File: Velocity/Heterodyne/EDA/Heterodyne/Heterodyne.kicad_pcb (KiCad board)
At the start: 2 copper layers, 39.5 x 29.5 mm, 40 parts, among them J1 I2C, J3 PWR, J4 Doppler_Out, J5 V_Square, J7 Reciever, U1 SA612AD, U2 NE5532, U3 MAX7375AXR105, U4 MAX11613

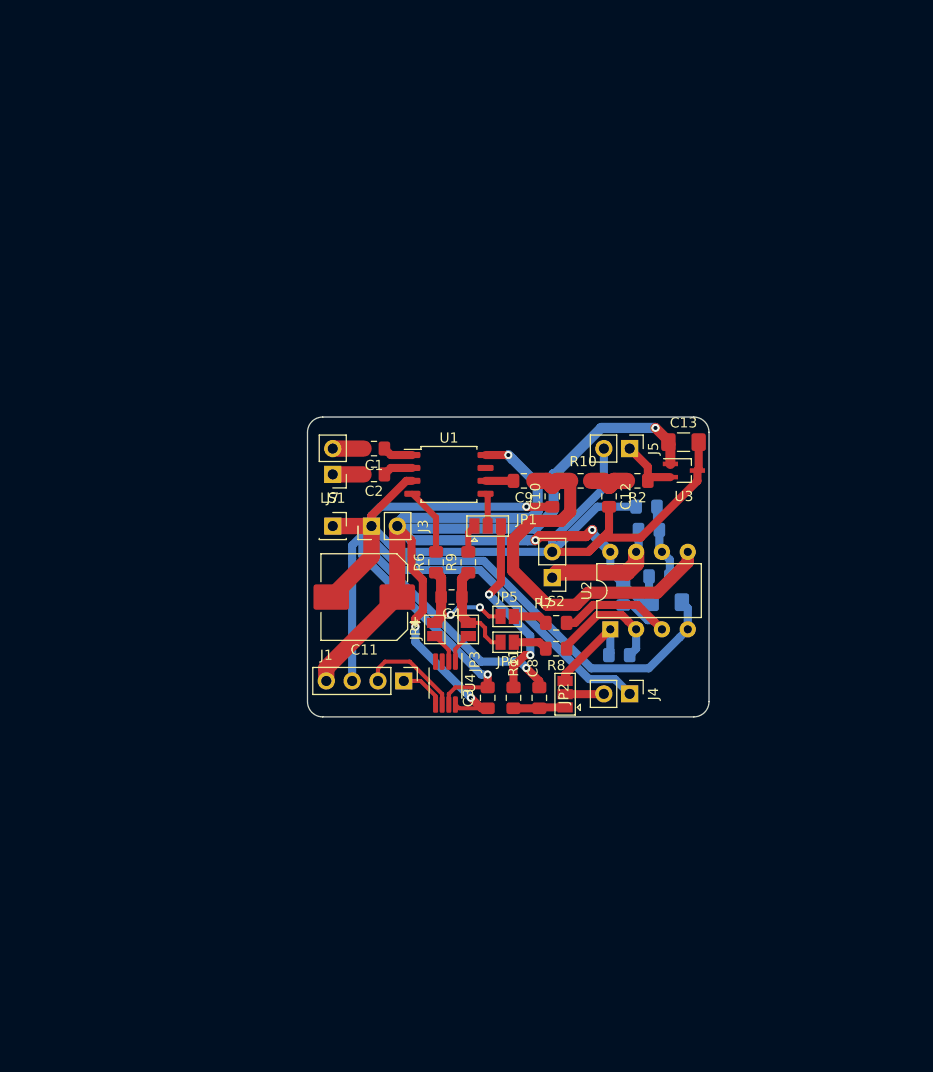
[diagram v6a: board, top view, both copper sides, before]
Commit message: added  ATmega328P to velocity schematic
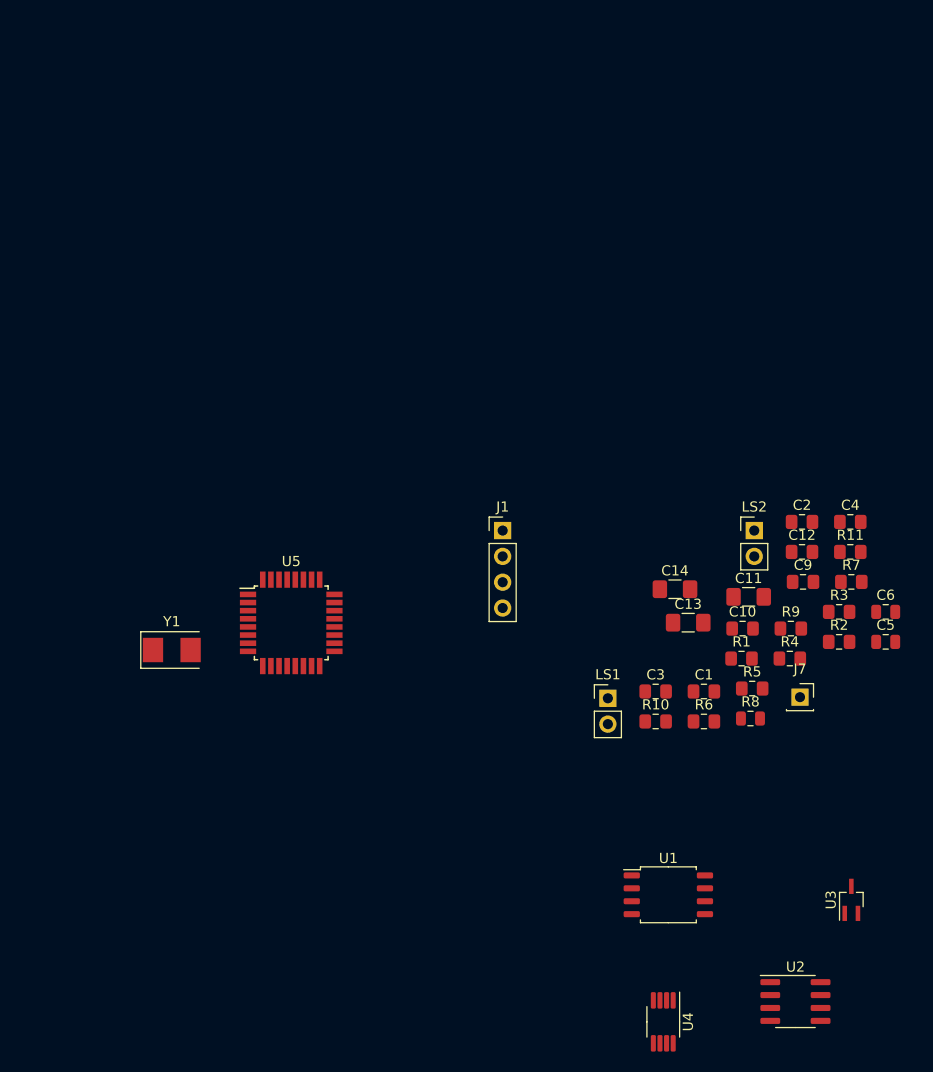
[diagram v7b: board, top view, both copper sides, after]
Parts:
- removed C8: 22 nF, Capacitor_SMD:C_0805_2012Metric_Pad1.15x1.40mm_HandSolder
- removed J3: PWR, Connector_PinHeader_2.54mm:PinHeader_1x02_P2.54mm_Vertical
- removed J4: Doppler_Out, Connector_PinHeader_2.54mm:PinHeader_1x02_P2.54mm_Vertical
- removed J5: V_Square, Connector_PinHeader_2.54mm:PinHeader_1x02_P2.54mm_Vertical
- removed JP1, JP2: Jumper_NC_Dual, Jumper:SolderJumper-3_P1.3mm_Open_Pad1.0x1.5mm
- removed JP3, JP4, JP5, JP6: SolderJumper_2_Open, Jumper:SolderJumper-2_P1.3mm_Open_Pad1.0x1.5mm
- removed R12: 18 kΩ, Resistor_SMD:R_0805_2012Metric_Pad1.15x1.40mm_HandSolder
- added C5: 22 nF, Capacitor_SMD:C_0805_2012Metric, F.Cu at (188.4, 97.1)
- added C6: 22 nF, Capacitor_SMD:C_0805_2012Metric, F.Cu at (188.4, 94.2)
- added U5: ATmega328PB-AU, Package_QFP:TQFP-32_7x7mm_P0.8mm, F.Cu at (129.9, 95.2)
- added Y1: 8 MHz, Crystal:Crystal_SMD_5032-2Pin_5.0x3.2mm, F.Cu at (118.2, 97.9)
- C11: value 330 μF -> 3.3 μF; footprint Capacitor_SMD:CP_Elec_8x10 -> Capacitor_SMD:C_1206_3216Metric_Pad1.42x1.75mm_HandSolder
- C14, R1, R3, R4: moved to F.Cu
- R11: value 330 Ω -> 20 kΩ
- R5: value 18 kΩ -> 2 kΩ; moved to F.Cu
- R6: value 330 Ω -> 1 kΩ
- R7: value 1 kΩ -> 330 Ω
- R8: value 1 kΩ -> 10 kΩ; footprint Resistor_SMD:R_0805_2012Metric_Pad1.15x1.40mm_HandSolder -> Resistor_SMD:R_0805_2012Metric
- U2: value NE5532 -> NE5532DR; footprint Package_DIP:DIP-8_W7.62mm -> Package_SO:SOIC-8_3.9x4.9mm_P1.27mm
- moved J7 49.0 mm to (179.9, 102.6)
- moved U1 46.6 mm to (167.0, 122.0)
- moved U3 45.3 mm to (185.0, 122.5), turned to 90 degrees
- moved C2 42.4 mm to (180.2, 85.3), turned to 0 degrees
- moved U2 40.9 mm to (179.5, 132.5), turned to 0 degrees
- moved C1 40.3 mm to (170.5, 102.0), turned to 0 degrees
- moved C4 39.9 mm to (184.9, 85.3), turned to 0 degrees
- moved U4 39.6 mm to (166.5, 134.5)
- moved C11 37.8 mm to (174.9, 92.7), turned to 0 degrees
- moved R11 36.1 mm to (184.9, 88.3), turned to 0 degrees
- moved LS1 34.9 mm to (161.1, 102.7), turned to 0 degrees
- moved R9 32.4 mm to (179.1, 95.8), turned to 0 degrees
- moved R6 30.7 mm to (170.5, 105.0), turned to 0 degrees
- moved R7 29.3 mm to (185.0, 91.2), turned to 0 degrees
- moved C9 29.2 mm to (180.2, 91.2), turned to 0 degrees
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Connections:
- C13 pad 2: VPP -> VCLOCK
- C14 pad 1: VPP -> VOPAMP
- J1 pad 1: Net-(J1-Pad1) -> BCLOCK
- J1 pad 2: Net-(J1-Pad2) -> BDATA
- R11 pad 1: Net-(C8-Pad1) -> SDA
- R11 pad 2: Net-(JP1-Pad3) -> VPP
- R5 pad 1: Net-(R5-Pad1) -> VPP
- R5 pad 2: VPP -> Net-(R5-Pad2)
- R6 pad 1: Net-(C4-Pad2) -> Net-(R5-Pad2)
- R6 pad 2: Net-(R6-Pad2) -> GND
- R7 pad 1: Net-(R5-Pad1) -> Net-(R7-Pad1)
- R7 pad 2: Net-(JP5-Pad2) -> Net-(C4-Pad1)
- R8 pad 1: Net-(R12-Pad1) -> VPP
- R9 pad 1: Net-(C4-Pad1) -> Net-(R9-Pad1)
- R9 pad 2: Net-(JP1-Pad1) -> Net-(C4-Pad2)
- U1 pad 4: Net-(R6-Pad2) -> Net-(R9-Pad1)
- U1 pad 5: Net-(JP1-Pad2) -> Net-(R7-Pad1)
- U2 pad 1: Net-(JP2-Pad3) -> (no net)
- U2 pad 2: Net-(R12-Pad1) -> (no net)
- U2 pad 3: Net-(R5-Pad1) -> (no net)
- U2 pad 8: VPP -> VOPAMP
- U3 pad 1: VPP -> VCLOCK
- U4 pad 1: Net-(JP3-Pad2) -> Net-(C4-Pad1)
- U4 pad 2: Net-(JP4-Pad2) -> Net-(C4-Pad2)
- U4 pad 4: Net-(U4-Pad4) -> Net-(R5-Pad2)
- U4 pad 5: Net-(J1-Pad1) -> SCL
- U4 pad 6: Net-(J1-Pad2) -> SDA
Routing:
- net GND: track 244.6 -> 0.00 mm, vias 3 -> 0
- net VPP: track 136.4 -> 0.00 mm, vias 6 -> 0
- net Driver_Wave: track 38.1 -> 0.00 mm
- net Net-(JP1-Pad3): track 19.0 -> 0.00 mm, vias 2 -> 0
- net Net-(R5-Pad1): track 15.9 -> 0.00 mm
- net Net-(LS2-Pad1): track 12.2 -> 0.00 mm
- net Net-(C4-Pad2): track 12.0 -> 0.00 mm, vias 2 -> 0
- net Net-(R12-Pad1): track 11.8 -> 0.00 mm
- net Net-(J1-Pad2): track 10.2 -> 0.00 mm
- net Net-(C4-Pad1): track 9.87 -> 0.00 mm
- net Net-(JP2-Pad3): track 9.52 -> 0.00 mm
- net Net-(R1-Pad2): track 7.38 -> 0.00 mm
- net Net-(R6-Pad2): track 6.68 -> 0.00 mm
- net Net-(R2-Pad1): track 6.28 -> 0.00 mm
- net Net-(C8-Pad1): track 5.12 -> 0.00 mm
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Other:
- board outline removed

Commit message: added 4 layer PCB for heterodyne
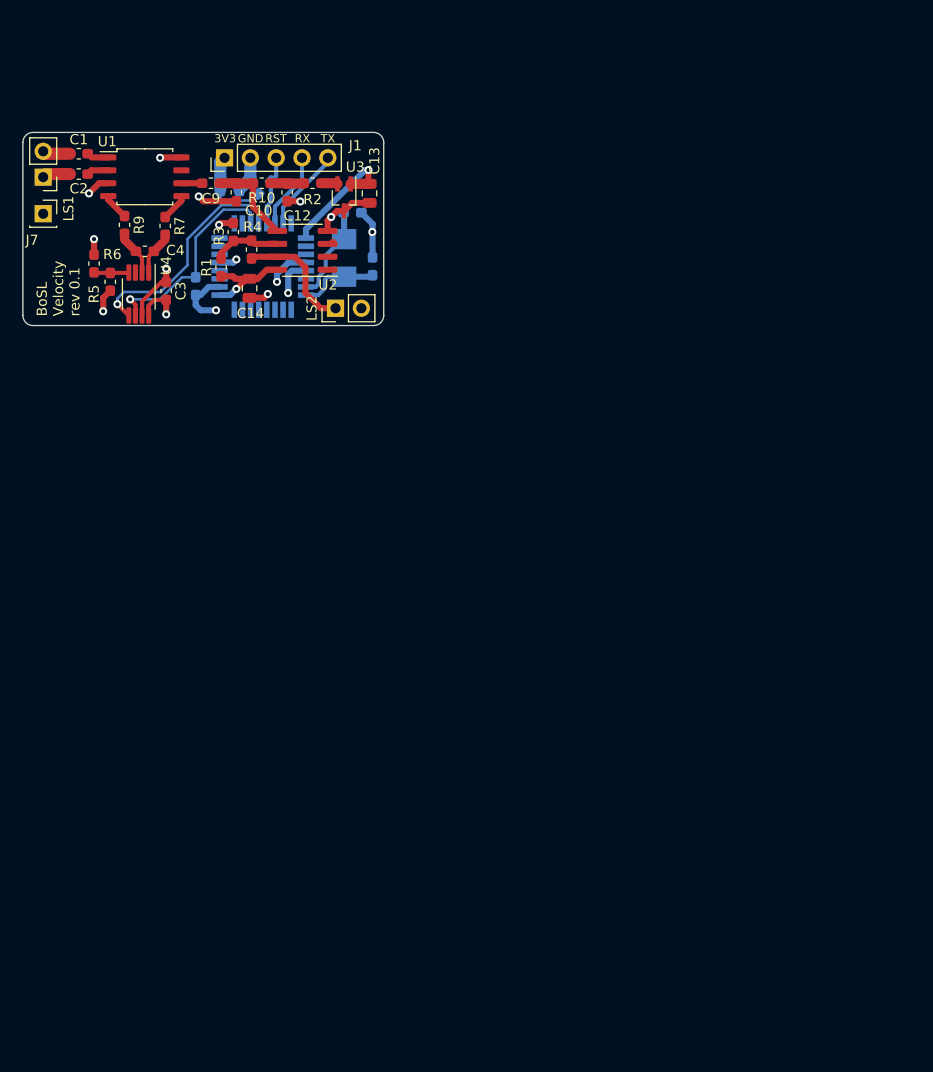
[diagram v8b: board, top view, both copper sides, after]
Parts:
- C1, C10, C12, C2, C3, C4, C9: footprint Capacitor_SMD:C_0805_2012Metric_Pad1.15x1.40mm_HandSolder -> Capacitor_SMD:C_0603_1608Metric_Pad1.05x0.95mm_HandSolder
- C11: footprint Capacitor_SMD:C_1206_3216Metric_Pad1.42x1.75mm_HandSolder -> Capacitor_SMD:C_0805_2012Metric; moved to B.Cu
- C13, C14: footprint Capacitor_SMD:C_1206_3216Metric_Pad1.42x1.75mm_HandSolder -> Capacitor_SMD:C_0805_2012Metric
- C5, C6: value 22 nF -> 18 pF; footprint Capacitor_SMD:C_0805_2012Metric -> Capacitor_SMD:C_0603_1608Metric_Pad1.05x0.95mm_HandSolder; moved to B.Cu
- J1: value I2C -> Conn_01x05; footprint Connector_PinHeader_2.54mm:PinHeader_1x04_P2.54mm_Vertical -> Connector_PinHeader_2.54mm:PinHeader_1x05_P2.54mm_Vertical
- R1, R10, R2, R3, R4, R5, R6, R7, R9: footprint Resistor_SMD:R_0805_2012Metric_Pad1.15x1.40mm_HandSolder -> Resistor_SMD:R_0603_1608Metric_Pad1.05x0.95mm_HandSolder
- R11: value 20 kΩ -> 10 kΩ; footprint Resistor_SMD:R_0805_2012Metric_Pad1.15x1.40mm_HandSolder -> Resistor_SMD:R_0603_1608Metric_Pad1.05x0.95mm_HandSolder; moved to B.Cu
- R8: footprint Resistor_SMD:R_0805_2012Metric -> Resistor_SMD:R_0603_1608Metric_Pad1.05x0.95mm_HandSolder; moved to B.Cu
- U5, Y1: moved to B.Cu
- moved U2 88.4 mm to (131.0, 58.6), turned to 180 degrees
- moved J7 88.3 mm to (105.5, 55.0)
- moved U4 88.3 mm to (114.9, 62.9)
- moved U1 87.4 mm to (115.5, 51.4)
- moved U3 85.2 mm to (135.1, 53.4), turned to 270 degrees
- moved C1 81.1 mm to (109.0, 49.1), turned to 180 degrees
- moved C2 79.0 mm to (109.0, 51.1), turned to 180 degrees
- moved R9 76.6 mm to (113.5, 56.1), turned to 270 degrees
- moved R7 76.0 mm to (117.5, 56.2), turned to 270 degrees
- moved LS1 75.6 mm to (105.5, 51.4), turned to 180 degrees
- moved R6 75.0 mm to (110.5, 59.9), turned to 90 degrees
- moved R5 74.8 mm to (112.1, 61.7), turned to 90 degrees
- moved C4 74.3 mm to (115.5, 58.7), turned to 180 degrees
- moved R8 70.8 mm to (127.3, 52.4), turned to 45 degrees
- moved R3 70.3 mm to (124.2, 56.8), turned to 270 degrees
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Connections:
- J1 pad 1: BCLOCK -> VPP
- J1 pad 2: BDATA -> GND
- J1 pad 3: GND -> TTL_RST
- J1 pad 4: VPP -> TTL_RX
- R1 pad 1: VPP -> VOPAMP
- R8 pad 2: Net-(R8-Pad2) -> TTL_RST
- U5 pad 1: Net-(U5-Pad1) -> VCLOCK
- U5 pad 10: BDATA -> Net-(U5-Pad10)
- U5 pad 11: BCLOCK -> Net-(U5-Pad11)
- U5 pad 17: Net-(U5-Pad17) -> VOPAMP
- U5 pad 18: Net-(U5-Pad18) -> VPP
- U5 pad 2: VOPAMP -> Net-(U5-Pad2)
- U5 pad 29: Net-(R8-Pad2) -> TTL_RST
- U5 pad 9: VCLOCK -> Net-(U5-Pad9)
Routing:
- net GND: track 0.00 -> 38.2 mm, vias 0 -> 11
- net VPP: track 0.00 -> 27.9 mm, vias 0 -> 5
- net SCL: track 0.00 -> 22.7 mm, vias 0 -> 1
- net SDA: track 0.00 -> 20.8 mm, vias 0 -> 1
- net VCLOCK: track 0.00 -> 12.7 mm, vias 0 -> 1
- net Net-(LS2-Pad1): track 0.00 -> 11.9 mm
- net VOPAMP: track 0.00 -> 9.82 mm, vias 0 -> 1
- net Net-(C5-Pad2): track 0.00 -> 9.55 mm
- net Driver_Wave: track 0.00 -> 8.96 mm
- net TTL_TX: track 0.00 -> 8.27 mm
- net Net-(C6-Pad1): track 0.00 -> 7.86 mm
- net TTL_RX: track 0.00 -> 7.55 mm
- net TTL_RST: track 0.00 -> 6.83 mm
- net Net-(R1-Pad2): track 0.00 -> 6.69 mm
- net Net-(C4-Pad2): track 0.00 -> 4.53 mm
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- added copper zone on In1.Cu, net GND
- added copper zone on In2.Cu, net VPP
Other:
- board outline added: 35.5 x 19 mm
- copper layers 2 -> 4
- board text added: "3V3"
- board text added: "BoSL Velocity rev 0.1"
- board text added: "GND"
- board text added: "RST"
- board text added: "RX"
- board text added: "TX"
